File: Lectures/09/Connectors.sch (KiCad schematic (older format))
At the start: 8 parts, among them J1 Serial, J2 Digital Pins, J3 I2C, J4 ICSP

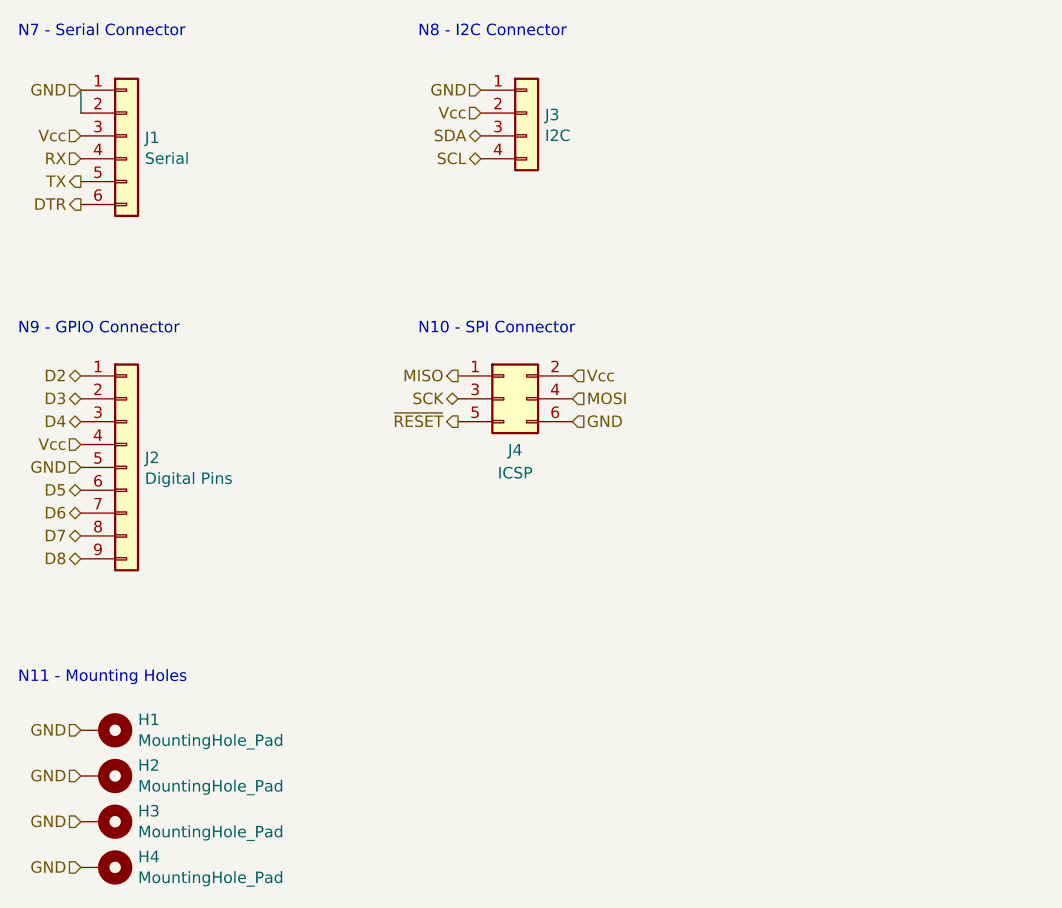
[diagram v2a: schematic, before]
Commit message: ATMEGA328 Layout
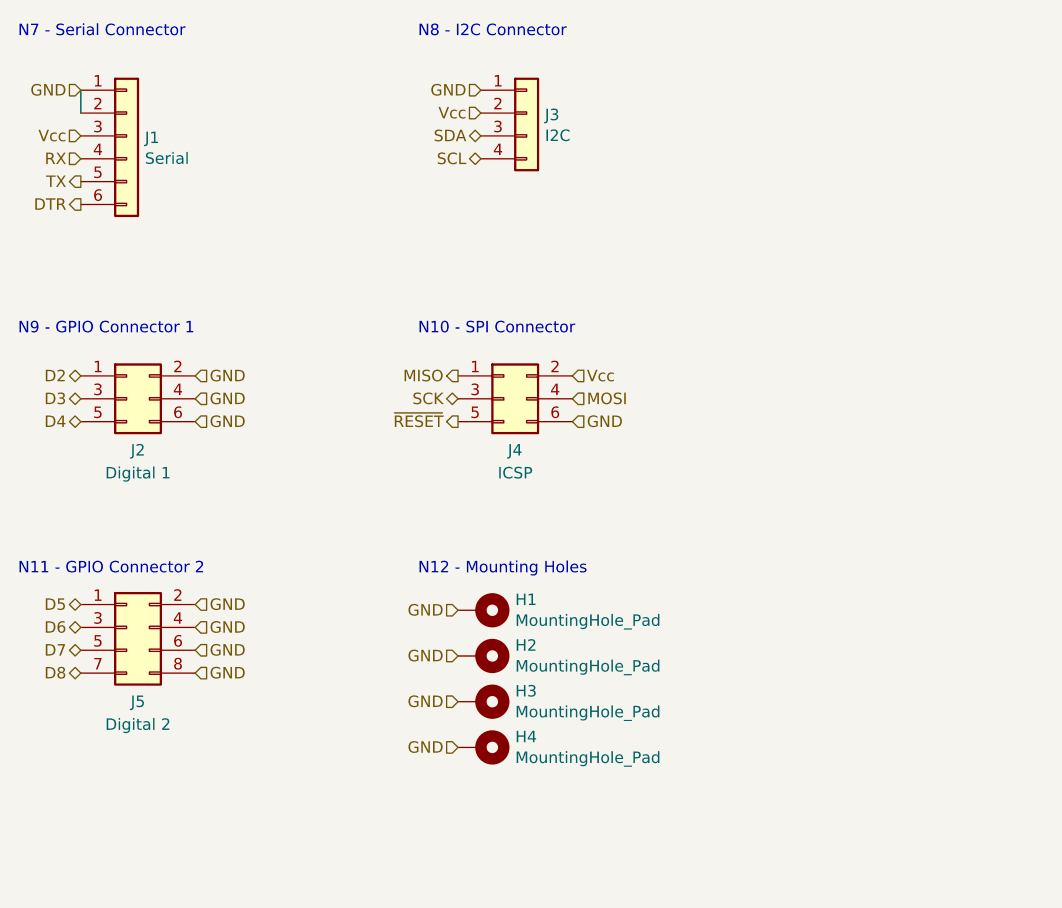
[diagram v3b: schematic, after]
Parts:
- removed J2: Digital Pins, Connector_PinSocket_2.54mm:PinSocket_1x09_P2.54mm_Vertical, symbol Connector_Generic:Conn_01x09
- added J2: Digital 1, Connector_PinSocket_2.54mm:PinSocket_2x03_P2.54mm_Vertical, symbol Connector_Generic:Conn_02x03_Odd_Even
- added J5: Digital 2, Connector_PinSocket_2.54mm:PinSocket_2x04_P2.54mm_Vertical, symbol Connector_Generic:Conn_02x04_Odd_Even
- H1, H2, H3, H4: footprint MountingHole:MountingHole_2.2mm_M2_Pad_Via -> MountingHole:MountingHole_2.2mm_M2_Pad
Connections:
- net D2: now also J2.1 (Pin_1)
- net D3: now also J2.3 (Pin_3)
- net D4: now also J2.5 (Pin_5)
- net D5: now also J5.1 (Pin_1)
- net D6: now also J5.3 (Pin_3)
- net D7: now also J5.5 (Pin_5)
- net D8: now also J5.7 (Pin_7)
- net GND: now also J2.2 (Pin_2), J2.4 (Pin_4), J2.6 (Pin_6), J5.2 (Pin_2), J5.4 (Pin_4), J5.6 (Pin_6), J5.8 (Pin_8)
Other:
- note added: "N11 - GPIO Connector 2"
- note added: "N12 - Mounting Holes"
- note added: "N9 - GPIO Connector 1"
- note removed: "N11 - Mounting Holes"
- note removed: "N9 - GPIO Connector"
- moved on the sheet: H1, H2, H3, H4
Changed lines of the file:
@@
 Text HLabel 6350 2850 0    50   BiDi ~ 0
 SCL
-Text HLabel 4600 3800 0    50   BiDi ~ 0
-D2
-Text HLabel 4600 3900 0    50   BiDi ~ 0
-D3
-Text HLabel 4600 4000 0    50   BiDi ~ 0
-D4
-Text HLabel 4600 4300 0    50   BiDi ~ 0
-D5
-Text HLabel 4600 4400 0    50   BiDi ~ 0
-D6
-Text HLabel 4600 4500 0    50   BiDi ~ 0
-D7
-Text HLabel 4600 4600 0    50   BiDi ~ 0
-D8
-Text HLabel 4600 4200 0    50   Input ~ 0
-GND
-Text HLabel 4600 4100 0    50   Input ~ 0
-Vcc
 Text Notes 4325 2325 0    50   ~ 0
 N7 - Serial Connector
@@
 N8 - I2C Connector
 Text Notes 4325 3625 0    50   ~ 0
-N9 - GPIO Connector
+N9 - GPIO Connector 1
 Text Notes 6075 3625 0    50   ~ 0
 N10 - SPI Connector
@@
 	1    0    0    -1
 $EndComp
-$Comp
-L Connector_Generic:Conn_01x09 J2
-U 1 1 601AA522
-P 4800 4200
-F 0 "J2" H 4880 4242 50  0000 L CNN
-F 1 "Digital Pins" H 4880 4151 50  0000 L CNN
-F 2 "Connector_PinSocket_2.54mm:PinSocket_1x09_P2.54mm_Vertical" H 4800 4200 50  0001 C CNN
-F 3 "~" H 4800 4200 50  0001 C CNN
-	1    4800 4200
-	1    0    0    -1
-$EndComp
 Wire Wire Line
 	4600 2650 4600 2550
@@
 L Mechanical:MountingHole_Pad H1
 U 1 1 6020F6BA
-P 4700 5350
-F 0 "H1" V 4654 5500 50  0000 L CNN
-F 1 "MountingHole_Pad" V 4745 5500 50  0000 L CNN
-F 2 "MountingHole:MountingHole_2.2mm_M2_Pad_Via" H 4700 5350 50  0001 C CNN
-F 3 "~" H 4700 5350 50  0001 C CNN
-	1    4700 5350
+P 6350 4825
+F 0 "H1" V 6304 4975 50  0000 L CNN
+F 1 "MountingHole_Pad" V 6395 4975 50  0000 L CNN
+F 2 "MountingHole:MountingHole_2.2mm_M2_Pad" H 6350 4825 50  0001 C CNN
+F 3 "~" H 6350 4825 50  0001 C CNN
+	1    6350 4825
 	0    1    1    0
 $EndComp
-Text HLabel 4600 5350 0    50   Input ~ 0
+Text HLabel 6250 4825 0    50   Input ~ 0
 GND
 $Comp
 L Mechanical:MountingHole_Pad H2
 U 1 1 602111E4
-P 4700 5550
-F 0 "H2" V 4654 5700 50  0000 L CNN
-F 1 "MountingHole_Pad" V 4745 5700 50  0000 L CNN
-F 2 "MountingHole:MountingHole_2.2mm_M2_Pad_Via" H 4700 5550 50  0001 C CNN
-F 3 "~" H 4700 5550 50  0001 C CNN
-	1    4700 5550
+P 6350 5025
+F 0 "H2" V 6304 5175 50  0000 L CNN
+F 1 "MountingHole_Pad" V 6395 5175 50  0000 L CNN
+F 2 "MountingHole:MountingHole_2.2mm_M2_Pad" H 6350 5025 50  0001 C CNN
+F 3 "~" H 6350 5025 50  0001 C CNN
+	1    6350 5025
 	0    1    1    0
 $EndComp
-Text HLabel 4600 5550 0    50   Input ~ 0
+Text HLabel 6250 5025 0    50   Input ~ 0
 GND
 $Comp
 L Mechanical:MountingHole_Pad H3
 U 1 1 6021157E
-P 4700 5750
-F 0 "H3" V 4654 5900 50  0000 L CNN
-F 1 "MountingHole_Pad" V 4745 5900 50  0000 L CNN
-F 2 "MountingHole:MountingHole_2.2mm_M2_Pad_Via" H 4700 5750 50  0001 C CNN
-F 3 "~" H 4700 5750 50  0001 C CNN
-	1    4700 5750
+P 6350 5225
+F 0 "H3" V 6304 5375 50  0000 L CNN
+F 1 "MountingHole_Pad" V 6395 5375 50  0000 L CNN
+F 2 "MountingHole:MountingHole_2.2mm_M2_Pad" H 6350 5225 50  0001 C CNN
+F 3 "~" H 6350 5225 50  0001 C CNN
+	1    6350 5225
 	0    1    1    0
 $EndComp
-Text HLabel 4600 5750 0    50   Input ~ 0
+Text HLabel 6250 5225 0    50   Input ~ 0
 GND
 $Comp
 L Mechanical:MountingHole_Pad H4
 U 1 1 60211856
-P 4700 5950
-F 0 "H4" V 4654 6100 50  0000 L CNN
-F 1 "MountingHole_Pad" V 4745 6100 50  0000 L CNN
-F 2 "MountingHole:MountingHole_2.2mm_M2_Pad_Via" H 4700 5950 50  0001 C CNN
-F 3 "~" H 4700 5950 50  0001 C CNN
-	1    4700 5950
+P 6350 5425
+F 0 "H4" V 6304 5575 50  0000 L CNN
+F 1 "MountingHole_Pad" V 6395 5575 50  0000 L CNN
+F 2 "MountingHole:MountingHole_2.2mm_M2_Pad" H 6350 5425 50  0001 C CNN
+F 3 "~" H 6350 5425 50  0001 C CNN
+	1    6350 5425
 	0    1    1    0
 $EndComp
-Text HLabel 4600 5950 0    50   Input ~ 0
+Text HLabel 6250 5425 0    50   Input ~ 0
 GND
-Text Notes 4325 5150 0    50   ~ 0
-N11 - Mounting Holes
+Text Notes 6075 4675 0    50   ~ 0
+N12 - Mounting Holes
+$Comp
+L Connector_Generic:Conn_02x03_Odd_Even J2
+U 1 1 6030EED1
+P 4800 3900
+F 0 "J2" H 4850 3675 50  0000 C CNN
+F 1 "Digital 1" H 4850 3575 50  0000 C CNN
+F 2 "Connector_PinSocket_2.54mm:PinSocket_2x03_P2.54mm_Vertical" H 4800 3900 50  0001 C CNN
+F 3 "~" H 4800 3900 50  0001 C CNN
+	1    4800 3900
+	1    0    0    -1
+$EndComp
+$Comp
+L Connector_Generic:Conn_02x04_Odd_Even J5
+U 1 1 6030F8C6
+P 4800 4900
+F 0 "J5" H 4850 4575 50  0000 C CNN
+F 1 "Digital 2" H 4850 4475 50  0000 C CNN
+F 2 "Connector_PinSocket_2.54mm:PinSocket_2x04_P2.54mm_Vertical" H 4800 4900 50  0001 C CNN
+F 3 "~" H 4800 4900 50  0001 C CNN
+	1    4800 4900
+	1    0    0    -1
+$EndComp
+Text HLabel 5100 5100 2    50   Input ~ 0
+GND
+Text HLabel 5100 5000 2    50   Input ~ 0
+GND
+Text HLabel 5100 4900 2    50   Input ~ 0
+GND
+Text HLabel 5100 4800 2    50   Input ~ 0
+GND
+Text HLabel 4600 5100 0    50   BiDi ~ 0
+D8
+Text HLabel 4600 5000 0    50   BiDi ~ 0
+D7
+Text HLabel 4600 4900 0    50   BiDi ~ 0
+D6
+Text HLabel 4600 4800 0    50   BiDi ~ 0
+D5
+Text HLabel 5100 4000 2    50   Input ~ 0
+GND
+Text HLabel 5100 3900 2    50   Input ~ 0
+GND
+Text HLabel 5100 3800 2    50   Input ~ 0
+GND
+Text HLabel 4600 4000 0    50   BiDi ~ 0
+D4
+Text HLabel 4600 3900 0    50   BiDi ~ 0
+D3
+Text HLabel 4600 3800 0    50   BiDi ~ 0
+D2
+Text Notes 4325 4675 0    50   ~ 0
+N11 - GPIO Connector 2
 $EndSCHEMATC
